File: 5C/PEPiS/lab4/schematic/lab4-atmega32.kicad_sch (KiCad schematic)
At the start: 54 parts, among them U1 ATmega32, X1 8MHz

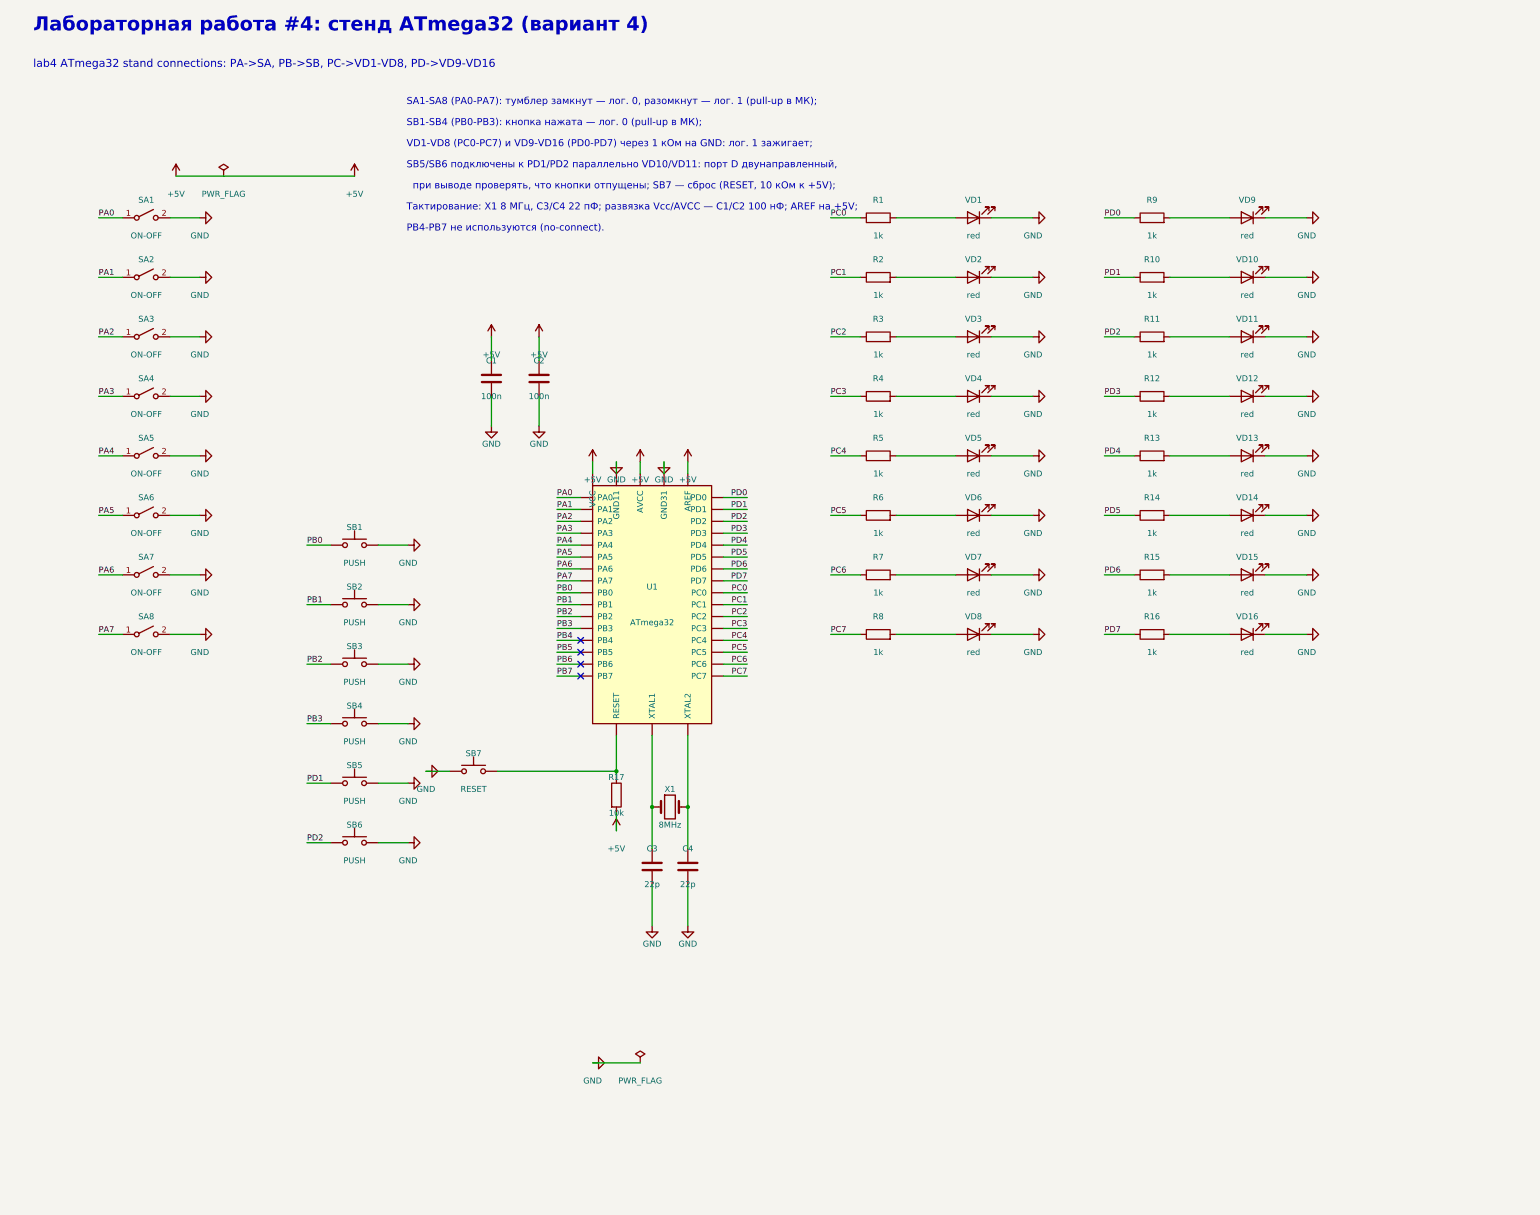
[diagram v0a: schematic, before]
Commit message: feat(lab4): checkpoint GUI schematic rework, add kicad project
User rail-splitting in progress after A3/footprint/title-block edits. ERC back to 0 errors / 2 warnings; PA0+PC4 copper short remains open. Add lab4-atmega32.kicad_pro so the sheet opens as a project.
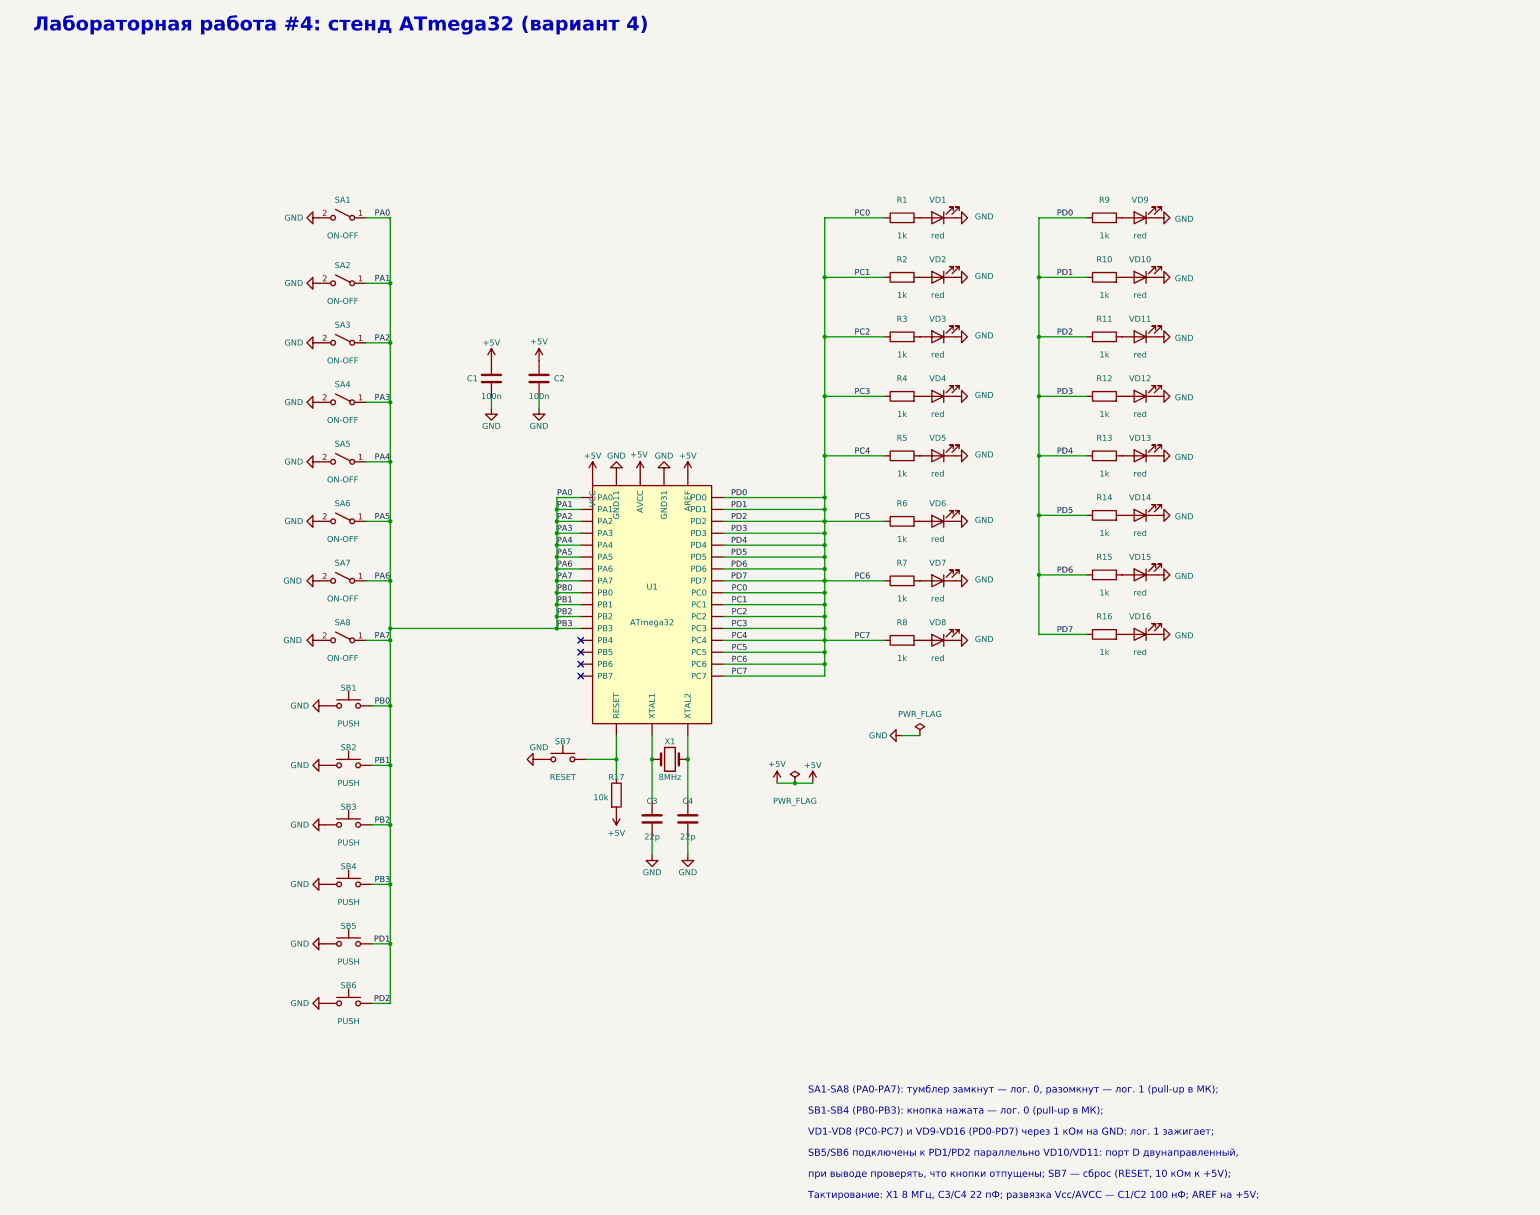
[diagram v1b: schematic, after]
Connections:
- net PA1 is gone; now on net PA0: SA2.1 (A), U1.39 (PA1)
- net PA2 is gone; now on net PA0: SA3.1 (A), U1.38 (PA2)
- net PA3 is gone; now on net PA0: SA4.1 (A), U1.37 (PA3)
- net PA4 is gone; now on net PA0: SA5.1 (A), U1.36 (PA4)
- net PA5 is gone; now on net PA0: SA6.1 (A), U1.35 (PA5)
- net PA6 is gone; now on net PA0: SA7.1 (A), U1.34 (PA6)
- net PA7 is gone; now on net PA0: SA8.1 (A), U1.33 (PA7)
- net PB0 is gone; now on net PA0: SB1.1, U1.1 (PB0)
- net PB1 is gone; now on net PA0: SB2.1, U1.2 (PB1)
- net PB2 is gone; now on net PA0: SB3.1, U1.3 (PB2)
- net PB3 is gone; now on net PA0: SB4.1, U1.4 (PB3)
- net PC0 is gone; now on net PA0: R1.1, U1.23 (PC0)
- net PC1 is gone; now on net PA0: R2.1, U1.22 (PC1)
- net PC2 is gone; now on net PA0: R3.1, U1.24 (PC2)
- net PC3 is gone; now on net PA0: R4.1, U1.25 (PC3)
- net PC4 is gone; now on net PA0: R5.1, U1.26 (PC4)
- net PC5 is gone; now on net PA0: R6.1, U1.27 (PC5)
- net PC6 is gone; now on net PA0: R7.1, U1.28 (PC6)
- net PC7 is gone; now on net PA0: R8.1, U1.29 (PC7)
- net PD0 is gone; now on net PA0: R9.1, U1.14 (PD0)
- net PD1 is gone; now on net PA0: R10.1, SB5.1, U1.15 (PD1)
- net PD2 is gone; now on net PA0: R11.1, SB6.1, U1.16 (PD2)
- net PD3 is gone; now on net PA0: R12.1, U1.17 (PD3)
- net PD4 is gone; now on net PA0: R13.1, U1.18 (PD4)
- net PD5 is gone; now on net PA0: R14.1, U1.19 (PD5)
- net PD6 is gone; now on net PA0: R15.1, U1.20 (PD6)
- net PD7 is gone; now on net PA0: R16.1, U1.21 (PD7)
- net PB4: no longer names the net of U1.5 (PB4)
- net PB5: no longer names the net of U1.6 (PB5)
- net PB6: no longer names the net of U1.7 (PB6)
- net PB7: no longer names the net of U1.8 (PB7)
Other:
- note removed: "PB4-PB7 не используются (no-connect)."
- note removed: "lab4 ATmega32 stand connections: PA->SA, PB->SB, PC->VD1-VD8, PD->VD9-VD16"
- moved on the sheet: C3, C4, R1, R10, R11, R12, R13, R14, R15, R16, R2, R3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

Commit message: feat(lab4): relocate notes block, refresh figure and report
Move schematic notes to bottom-left, clearing the PC0/PD0 top rows. ERC 0 errors / 1 warning. Rebuild report.docx with the whole-sheet figure.
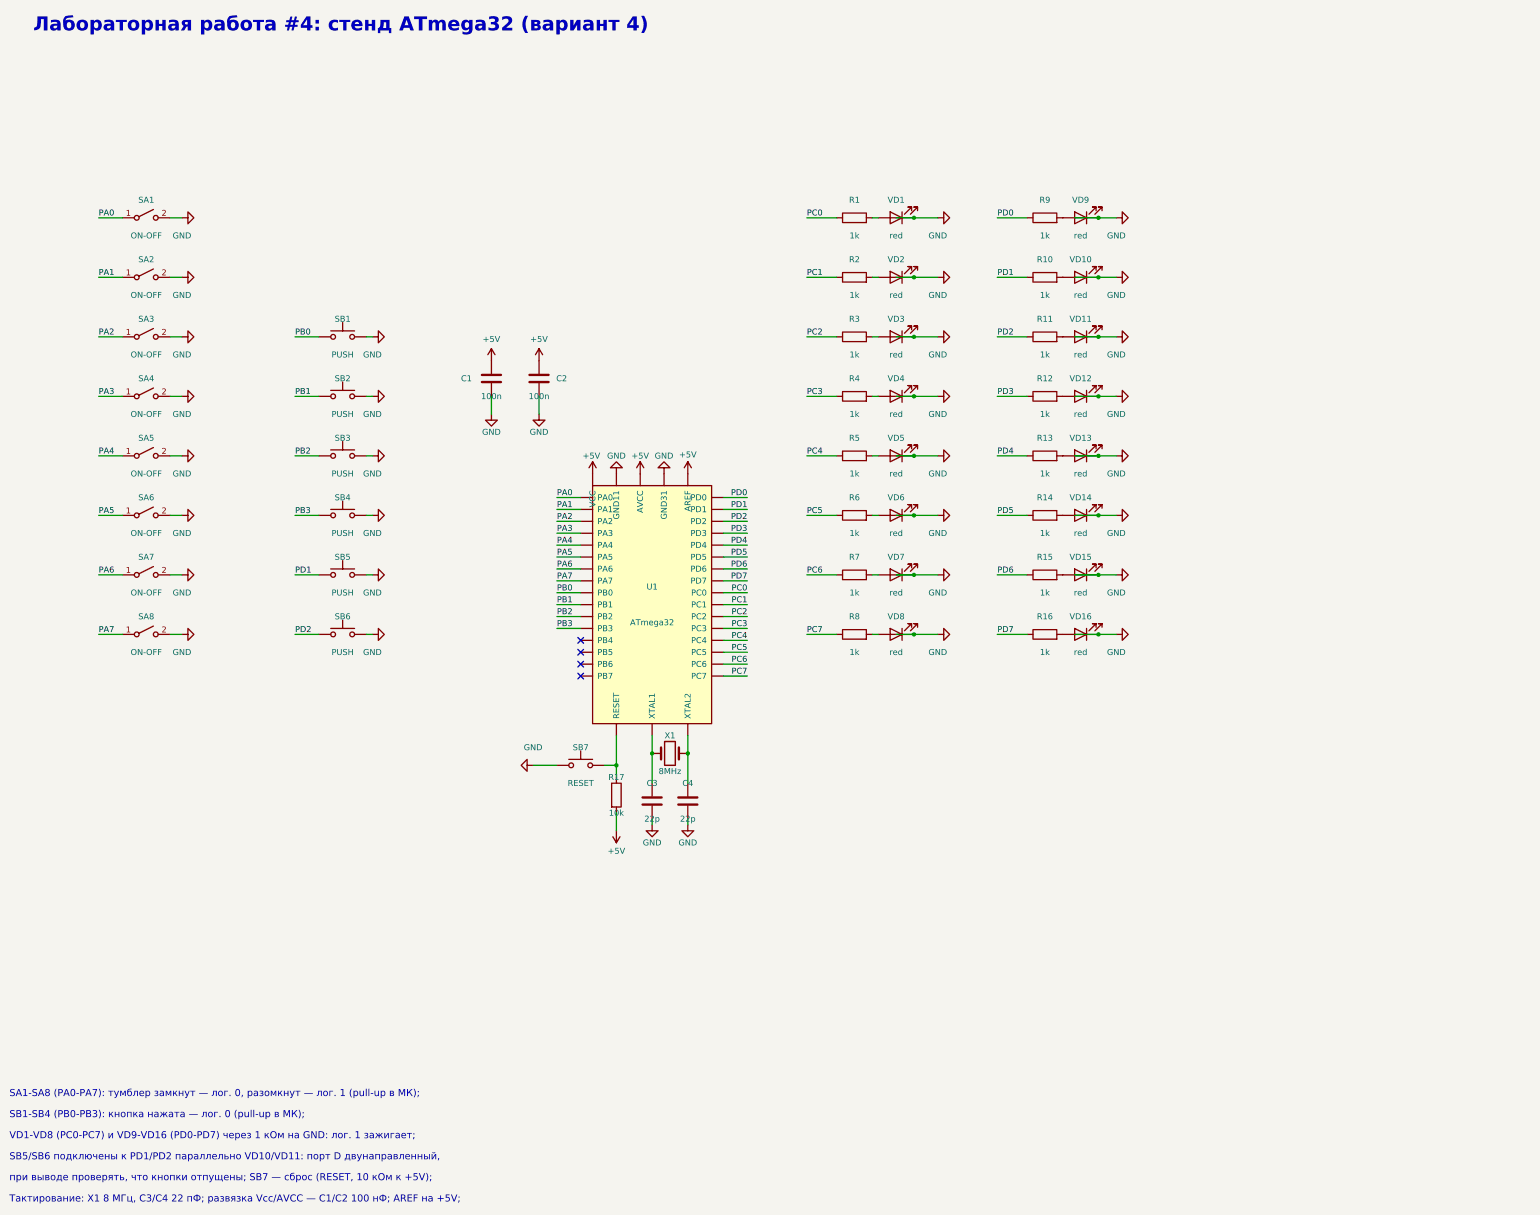
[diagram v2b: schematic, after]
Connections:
- net PA0: no longer R1.1, R10.1, R11.1, R12.1, R13.1, R14.1, R15.1, R16.1, R2.1, R3.1, R4.1, R5.1, R6.1, R7.1, R8.1, R9.1, SA2.1 (A), SA3.1 (A), SA4.1 (A), SA5.1 (A), SA6.1 (A), SA7.1 (A), SA8.1 (A), SB1.1, SB2.1, SB3.1, SB4.1, SB5.1, SB6.1, U1.1 (PB0), U1.14 (PD0), U1.15 (PD1), U1.16 (PD2), U1.17 (PD3), U1.18 (PD4), U1.19 (PD5), U1.2 (PB1), U1.20 (PD6), U1.21 (PD7), U1.22 (PC1), U1.23 (PC0), U1.24 (PC2), U1.25 (PC3), U1.26 (PC4), U1.27 (PC5), U1.28 (PC6), U1.29 (PC7), U1.3 (PB2), U1.33 (PA7), U1.34 (PA6), U1.35 (PA5), U1.36 (PA4), U1.37 (PA3), U1.38 (PA2), U1.39 (PA1), U1.4 (PB3)
- new net PA1: SA2.1 (A), U1.39 (PA1)
- new net PA2: SA3.1 (A), U1.38 (PA2)
- new net PA3: SA4.1 (A), U1.37 (PA3)
- new net PA4: SA5.1 (A), U1.36 (PA4)
- new net PA5: SA6.1 (A), U1.35 (PA5)
- new net PA6: SA7.1 (A), U1.34 (PA6)
- new net PA7: SA8.1 (A), U1.33 (PA7)
- new net PB0: SB1.1, U1.1 (PB0)
- new net PB1: SB2.1, U1.2 (PB1)
- new net PB2: SB3.1, U1.3 (PB2)
- new net PB3: SB4.1, U1.4 (PB3)
- new net PC0: R1.1, U1.23 (PC0)
- new net PC1: R2.1, U1.22 (PC1)
- new net PC2: R3.1, U1.24 (PC2)
- new net PC3: R4.1, U1.25 (PC3)
- new net PC4: R5.1, U1.26 (PC4)
- new net PC5: R6.1, U1.27 (PC5)
- new net PC6: R7.1, U1.28 (PC6)
- new net PC7: R8.1, U1.29 (PC7)
- new net PD0: R9.1, U1.14 (PD0)
- new net PD1: R10.1, SB5.1, U1.15 (PD1)
- new net PD2: R11.1, SB6.1, U1.16 (PD2)
- new net PD3: R12.1, U1.17 (PD3)
- new net PD4: R13.1, U1.18 (PD4)
- new net PD5: R14.1, U1.19 (PD5)
- new net PD6: R15.1, U1.20 (PD6)
- new net PD7: R16.1, U1.21 (PD7)
